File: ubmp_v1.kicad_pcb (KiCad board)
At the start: 2 copper layers, 29 x 12 mm, 25 parts, among them J1 M20-9760542, P1 USB_C_Plug, U1 NUF8401MNT4G, U2 MIC5245-3.3YM5, U3 STM32F103CBU6, U4 NUF2042XV6T1G, Y1 PRQC8.00CR1010V00L

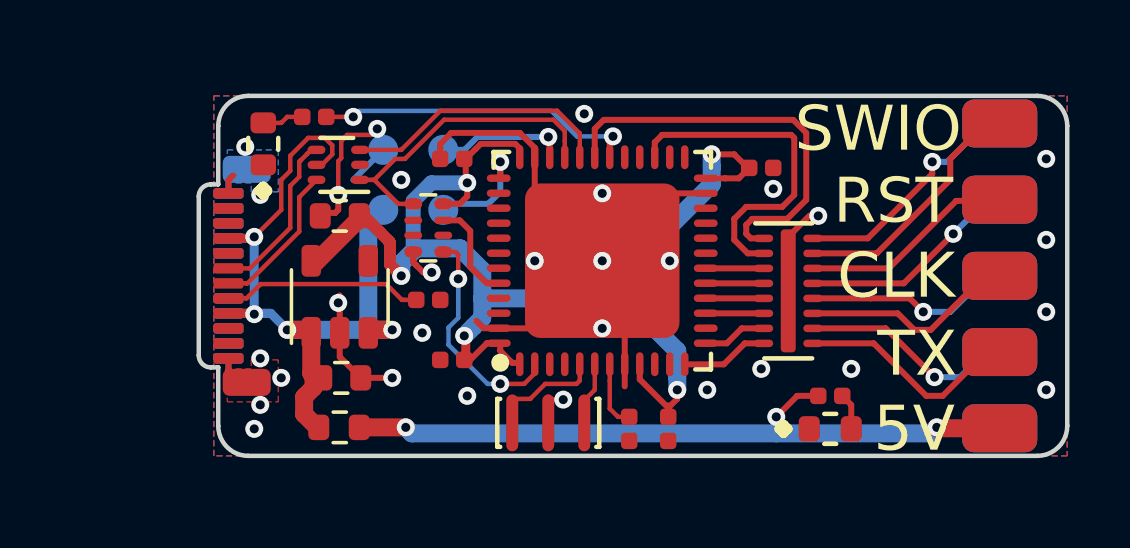
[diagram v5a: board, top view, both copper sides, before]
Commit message: Fixed corners to better fit the USB-C connector
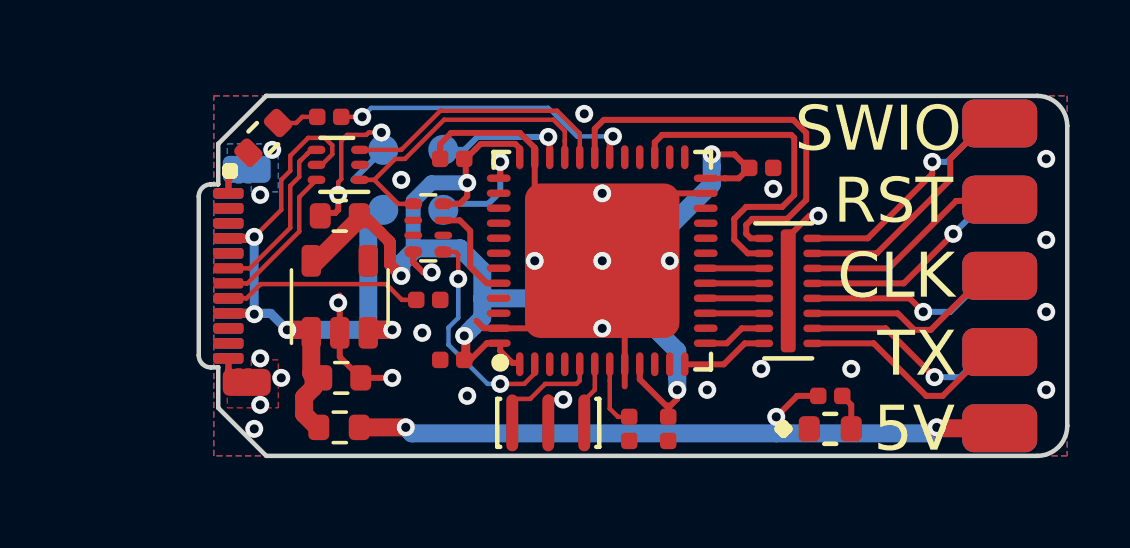
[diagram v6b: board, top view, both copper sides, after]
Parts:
- moved R1 0.50 mm to (93.9, 100.7)
- moved D1 0.20 mm to (91.7, 101.4), turned to 45 degrees
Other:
- outline, holes or cut-outs redrawn
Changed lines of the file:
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@@
     (thickness 0.7)
     (drawings 33)
-    (tracks 367)
+    (tracks 368)
     (zones 0)
     (modules 25)
@@
   )
   (module leds:LEDC1608X60 (layer F.Cu)
-    (at 91.7 101.6 90)
+    (at 91.7 101.4 45)
     (descr "LED,Chip;1.60mm L X 0.80mm W X 0.60mm H")
     (attr smd)
-    (fp_text reference D1 (at -1.6 0.75 90) (layer F.SilkS) hide
-      (effects (font (size 0.6 0.6) (thickness 0.13)))
-    )
-    (fp_text value LTST-C191KGKT (at 0 0.7 90) (layer F.Fab)
+    (fp_text reference D1 (at -1.6 0.75 45) (layer F.SilkS) hide
+      (effects (font (size 0.6 0.6) (thickness 0.13)))
+    )
+    (fp_text value LTST-C191KGKT (at 0 0.7 45) (layer F.Fab)
       (effects (font (size 0.3 0.3) (thickness 0.05)))
     )
@@
     (fp_line (start 0.95 0.35) (end -0.95 0.35) (layer F.Fab) (width 0.15))
     (fp_line (start -0.95 -0.1) (end -0.7 -0.35) (layer F.Fab) (width 0.15))
-    (fp_text user %R (at 0 0 270) (layer F.Fab)
+    (fp_text user %R (at 0 0 225) (layer F.Fab)
       (effects (font (size 0.4 0.4) (thickness 0.075)))
     )
-    (pad 2 smd roundrect (at 0.7 0 90) (size 0.7 0.85) (layers F.Cu F.Paste F.Mask) (roundrect_rratio 0.25)
+    (pad 2 smd roundrect (at 0.7 0 45) (size 0.7 0.85) (layers F.Cu F.Paste F.Mask) (roundrect_rratio 0.25)
       (net 11 "Net-(D1-Pad2)"))
-    (pad 1 smd roundrect (at -0.7 0 90) (size 0.7 0.85) (layers F.Cu F.Paste F.Mask) (roundrect_rratio 0.25)
+    (pad 1 smd roundrect (at -0.7 0 45) (size 0.7 0.85) (layers F.Cu F.Paste F.Mask) (roundrect_rratio 0.25)
       (net 2 GND))
     (model ${KIPRJMOD}/kicad_libs/3dmodels/step/LED_0603_G.STEP
@@
   )
   (module passive:R_0402_1005Metric_Rounded (layer F.Cu)
-    (at 93.4 100.7 180)
+    (at 93.9 100.7 180)
     (descr "Resistor SMD 0402 (1005 Metric), square (rectangular) end terminal, IPC_7351 nominal, (Body size source: http://www.tortai-tech.com/upload/download/2011102023233369053.pdf), generated with kicad-footprint-generator")
     (tags resistor)
@@
       (net 3 +5V))
   )
-  (gr_arc (start 91.2 101) (end 91.2 100) (angle -90) (layer Edge.Cuts) (width 0.15))
-  (gr_arc (start 91.2 111) (end 90.2 111) (angle -90) (layer Edge.Cuts) (width 0.15))
+  (gr_line (start 91.8 112) (end 90.2 110.4) (layer Edge.Cuts) (width 0.15))
+  (gr_line (start 90.2 101.6) (end 91.8 100) (layer Edge.Cuts) (width 0.15))
   (gr_arc (start 89.95 108.65) (end 89.55 108.65) (angle -90) (layer Edge.Cuts) (width 0.15))
   (gr_arc (start 89.95 103.35) (end 89.95 102.95) (angle -90) (layer Edge.Cuts) (width 0.15))
-  (gr_line (start 90.2 109.05) (end 90.2 111) (layer Edge.Cuts) (width 0.15))
+  (gr_line (start 90.2 109.05) (end 90.2 110.4) (layer Edge.Cuts) (width 0.15))
   (gr_line (start 89.95 109.05) (end 90.2 109.05) (layer Edge.Cuts) (width 0.15))
   (gr_line (start 89.55 103.35) (end 89.55 108.65) (layer Edge.Cuts) (width 0.15))
   (gr_line (start 90.2 102.95) (end 89.95 102.95) (layer Edge.Cuts) (width 0.15))
-  (gr_line (start 90.2 101) (end 90.2 102.95) (layer Edge.Cuts) (width 0.15))
+  (gr_line (start 90.2 101.6) (end 90.2 102.95) (layer Edge.Cuts) (width 0.15))
   (gr_arc (start 117.5 111) (end 117.5 112) (angle -90) (layer Edge.Cuts) (width 0.15))
   (gr_arc (start 117.5 101) (end 118.5 101) (angle -90) (layer Edge.Cuts) (width 0.15))
@@
     (effects (font (size 1.5 1.5) (thickness 0.3)))
   )
-  (gr_line (start 91.2 100) (end 117.5 100) (layer Edge.Cuts) (width 0.15))
-  (gr_line (start 91.2 112) (end 117.5 112) (layer Edge.Cuts) (width 0.15))
+  (gr_line (start 91.8 100) (end 117.5 100) (layer Edge.Cuts) (width 0.15))
+  (gr_line (start 91.8 112) (end 117.5 112) (layer Edge.Cuts) (width 0.15))
   (gr_text "3.3V ONLY" (at 104.6 103.8) (layer B.SilkS)
     (effects (font (size 1.3 1.3) (thickness 0.25)) (justify mirror))
@@
   (via (at 96.3 102.8) (size 0.6) (drill 0.3) (layers F.Cu B.Cu) (net 2))
   (via (at 102.4 100.6) (size 0.6) (drill 0.3) (layers F.Cu B.Cu) (net 2))
-  (segment (start 94.2 103.3) (end 94.2 102.175483) (width 0.15) (layer F.Cu) (net 2))
-  (via (at 95.5 101.1) (size 0.6) (drill 0.3) (layers F.Cu B.Cu) (net 2))
-  (segment (start 94.2 102.175483) (end 94.30002 102.075463) (width 0.15) (layer F.Cu) (net 2))
-  (segment (start 94.30002 102.075463) (end 94.30002 101.50002) (width 0.15) (layer F.Cu) (net 2))
-  (segment (start 94.50004 101.3) (end 95.3 101.3) (width 0.15) (layer F.Cu) (net 2))
-  (segment (start 94.30002 101.50002) (end 94.50004 101.3) (width 0.15) (layer F.Cu) (net 2))
-  (segment (start 95.3 101.3) (end 95.5 101.1) (width 0.15) (layer F.Cu) (net 2))
   (segment (start 97.965517 101.234483) (end 97.6 101.6) (width 0.2) (layer F.Cu) (net 2))
   (segment (start 97.6 102.05) (end 97.55 102.1) (width 0.2) (layer F.Cu) (net 2))
@@
   (via (at 91.6 110.3) (size 0.6) (drill 0.3) (layers F.Cu B.Cu) (net 2))
   (via (at 92.3 109.4) (size 0.6) (drill 0.3) (layers F.Cu B.Cu) (net 2))
-  (via (at 91.1 101.7) (size 0.6) (drill 0.3) (layers F.Cu B.Cu) (net 2))
+  (via (at 92 101.8) (size 0.6) (drill 0.3) (layers F.Cu B.Cu) (net 2))
   (segment (start 90.54 103.25) (end 90.54 102.81) (width 0.2) (layer F.Cu) (net 2))
   (segment (start 90.54 102.81) (end 90.7 102.65) (width 0.2) (layer F.Cu) (net 2))
@@
   (segment (start 90.54 108.75) (end 90.54 109.14) (width 0.2) (layer B.Cu) (net 2))
   (segment (start 90.54 109.14) (end 90.7 109.3) (width 0.2) (layer B.Cu) (net 2))
+  (segment (start 94.30002 101.50002) (end 94.50004 101.3) (width 0.15) (layer F.Cu) (net 2))
+  (segment (start 94.30002 102.775716) (end 94.30002 101.50002) (width 0.15) (layer F.Cu) (net 2))
+  (segment (start 95.21551 101.220733) (end 95.639774 101.220733) (width 0.15) (layer F.Cu) (net 2))
+  (segment (start 94.2 102.875736) (end 94.30002 102.775716) (width 0.15) (layer F.Cu) (net 2))
+  (segment (start 95.136243 101.3) (end 95.21551 101.220733) (width 0.15) (layer F.Cu) (net 2))
+  (segment (start 94.2 103.3) (end 94.2 102.875736) (width 0.15) (layer F.Cu) (net 2))
+  (via (at 95.639774 101.220733) (size 0.6) (drill 0.3) (layers F.Cu B.Cu) (net 2))
+  (segment (start 94.50004 101.3) (end 95.136243 101.3) (width 0.15) (layer F.Cu) (net 2))
   (segment (start 93.45 109.4) (end 93.3 109.25) (width 0.6) (layer F.Cu) (net 3))
   (segment (start 93.3 109.25) (end 93.3 107.9) (width 0.6) (layer F.Cu) (net 3))
@@
   (segment (start 100.75 108.945) (end 100.75 109.25) (width 0.15) (layer F.Cu) (net 10))
   (segment (start 100.75 109.25) (end 100.4 109.6) (width 0.15) (layer F.Cu) (net 10))
-  (segment (start 92.5 100.7) (end 93 100.7) (width 0.15) (layer F.Cu) (net 11))
-  (segment (start 91.7 100.9) (end 92.3 100.9) (width 0.15) (layer F.Cu) (net 11))
-  (segment (start 92.3 100.9) (end 92.5 100.7) (width 0.15) (layer F.Cu) (net 11))
+  (segment (start 92.794975 100.905025) (end 92.194975 100.905025) (width 0.15) (layer F.Cu) (net 11))
+  (segment (start 93.5 100.7) (end 93 100.7) (width 0.15) (layer F.Cu) (net 11))
+  (segment (start 93 100.7) (end 92.794975 100.905025) (width 0.15) (layer F.Cu) (net 11))
   (via (at 103.357273 101.35001) (size 0.6) (drill 0.3) (layers F.Cu B.Cu) (net 12))
   (segment (start 103.34499 101.35001) (end 103.357273 101.35001) (width 0.2) (layer F.Cu) (net 12))
   (segment (start 103.25 101.445) (end 103.34499 101.35001) (width 0.2) (layer F.Cu) (net 12))
   (segment (start 103.25 102.045) (end 103.25 101.445) (width 0.2) (layer F.Cu) (net 12))
-  (via (at 94.7 100.7) (size 0.6) (drill 0.3) (layers F.Cu B.Cu) (net 12))
-  (segment (start 93.8 100.7) (end 94.7 100.7) (width 0.15) (layer F.Cu) (net 12))
-  (segment (start 102.15001 101.35001) (end 103.357273 101.35001) (width 0.15) (layer B.Cu) (net 12))
-  (segment (start 101.3 100.5) (end 102.15001 101.35001) (width 0.15) (layer B.Cu) (net 12))
-  (segment (start 94.7 100.7) (end 94.9 100.5) (width 0.15) (layer B.Cu) (net 12))
-  (segment (start 94.9 100.5) (end 101.3 100.5) (width 0.15) (layer B.Cu) (net 12))
+  (segment (start 102.15001 101.35001) (end 101.200001 100.400001) (width 0.15) (layer B.Cu) (net 12))
+  (segment (start 101.200001 100.400001) (end 95.300017 100.400001) (width 0.15) (layer B.Cu) (net 12))
+  (segment (start 95.300017 100.400001) (end 95.000018 100.7) (width 0.15) (layer B.Cu) (net 12))
+  (via (at 95.000018 100.7) (size 0.6) (drill 0.3) (layers F.Cu B.Cu) (net 12))
+  (segment (start 103.357273 101.35001) (end 102.15001 101.35001) (width 0.15) (layer B.Cu) (net 12))
+  (segment (start 95.000018 100.7) (end 94.3 100.7) (width 0.15) (layer F.Cu) (net 12))
   (segment (start 95.3 102.8) (end 94.925 102.8) (width 0.15) (layer F.Cu) (net 13))
   (segment (start 95.4 102.8) (end 95.3 102.8) (width 0.15) (layer F.Cu) (net 13))
@@
     (polygon
       (pts
-        (xy 90.5 110.2) (xy 92.2 110.2) (xy 92.2 108.8) (xy 91.3 108.8) (xy 91.3 109.1)
+        (xy 90.5 110.4) (xy 92.2 110.4) (xy 92.2 108.8) (xy 91.3 108.8) (xy 91.3 109.1)
         (xy 90.5 109.1)
       )
@@
     (polygon
       (pts
-        (xy 90.5 101.8) (xy 92.2 101.8) (xy 92.2 103.2) (xy 91.3 103.2) (xy 91.3 102.9)
+        (xy 90.5 101.6) (xy 92.2 101.6) (xy 92.2 103.2) (xy 91.3 103.2) (xy 91.3 102.9)
         (xy 90.5 102.9)
       )
